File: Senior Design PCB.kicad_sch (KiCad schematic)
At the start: 49 parts, among them J1 Conn_01x02_Shielded, J2 Conn_01x02_Shielded, J3 Raspberry_Pi_Zero_2W, J4 Conn_01x02, J4(DISPLAY)1 Conn_01x09, J5 Conn_01x02, J6 Conn_01x02, U1 LM2596S-5, U2 MAX38890, U3 MCP3008

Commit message: More footprints added.
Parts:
- removed J1, J2: Conn_01x02_Shielded, symbol Connector_Generic_Shielded:Conn_01x02_Shielded
- removed J4(DISPLAY)1: Conn_01x09, symbol Connector_Generic:Conn_01x09
- removed U1: LM2596S-5, Package_TO_SOT_SMD:TO-263-5_TabPin3, symbol Regulator_Switching:LM2596S-5
- added H1, H2, H3, H4: MountingHole_Pad, MountingHole:MountingHole_3.2mm_M3_Pad, symbol Mechanical:MountingHole_Pad
- added J1, J2, TP2: Conn_01x02, Connector_PinHeader_2.54mm:PinHeader_1x02_P2.54mm_Vertical, symbol Connector_Generic:Conn_01x02
- added J7-A1: Conn_01x05, Connector_PinSocket_2.54mm:PinSocket_1x05_P2.54mm_Vertical, symbol Connector_Generic:Conn_01x05
- added J7-B1: Conn_01x04, Connector_PinSocket_2.54mm:PinSocket_1x04_P2.54mm_Vertical, symbol Connector_Generic:Conn_01x04
- added U1: LM2678SX-5.0/NOPB, TS7B, symbol AAA_Senior_Design:LM2678SX-5.0_NOPB
- BKB1, CAP1, ENB1, ENC1, FBCH1, FBCR1, FBS1, ISET1, LX1, RDY1, SYS1, VOUT1: footprint (none) -> Connector_Wire:SolderWire-1sqmm_1x02_P5.4mm_D1.4mm_OD2.7mm
- C1: renamed from C10; value 56uF -> 100uF; footprint (none) -> Capacitor_THT:CP_Radial_D8.0mm_P2.50mm
- C2: renamed from C12; footprint Capacitor_SMD:C_1206_3216Metric -> Capacitor_THT:CP_Radial_D5.0mm_P2.50mm
- C3: renamed from C7; footprint (none) -> Capacitor_THT:CP_Radial_D5.0mm_P2.00mm
- C5: renamed from C9; value 3.3nF -> 10nF; footprint (none) -> Capacitor_THT:CP_Radial_D10.0mm_P3.80mm
- C6: renamed from C13; footprint Capacitor_SMD:C_1206_3216Metric -> Capacitor_THT:CP_Radial_D5.0mm_P2.50mm
- C7: renamed from C11; value 330.0uF -> 220.0uF
- D1: value D_Schottky -> 40V; footprint (none) -> AAA_senior_design:D2PAK_STM
- L1: renamed from L2; value 47.0uH -> 15uH; footprint (none) -> AAA_senior_design:15uHInductor
- TP1: renamed from J4; footprint (none) -> Connector_Wire:SolderWire-1sqmm_1x02_P5.4mm_D1.4mm_OD2.7mm
- TP3: renamed from J5; footprint (none) -> Connector_Wire:SolderWire-1sqmm_1x02_P5.4mm_D1.4mm_OD2.7mm
- TP4: renamed from J6; footprint (none) -> Connector_Wire:SolderWire-1sqmm_1x02_P5.4mm_D1.4mm_OD2.7mm
- renumbered C4 to C10, C3 to C11, C5 to C12, C6 to C13, C8 to C4, C1 to C8, C2 to C9, L1 to L2, R5 to R1, R1 to R2, R2 to R3, R3 to R4, R4 to R5, R8 to R6, R9 to R7, R6 to R8, R7 to R9, U3 to U2, U2 to U3
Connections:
- net 12V: now also C2.2, U1.2 (VIN); no longer C1.1
- net 5V: now also U1.6 (FB); no longer C5.2
- net GND: now also H1.1, H2.1, H3.1, H4.1, J1.1 (Pin_1), J2.1 (Pin_1), J7-B1.4 (Pin_4), U1.4 (GND), U1.5 (NC), U1.8 (TAB); no longer C5.1
- net Vsig: now also J2.2 (Pin_2)
- net at D1.1 (K), L1.1: now also C5.2, U1.1 (VSW)
- net at TP1.1 (Pin_1): now also C1.1, J1.2 (Pin_2); no longer C2.2
- net at J3.2 (5V), U2.15 (Vref), U2.16 (Vdd): now also J7-A1.1 (Pin_1)
- net at J3.12 (SPI1_CE0): now also J7-A1.2 (Pin_2)
- net at J3.16 (RST): now also J7-A1.3 (Pin_3)
- net at J3.18 (GPIO24): now also J7-A1.4 (Pin_4)
- net at J3.29 (KEY1): now also J7-A1.5 (Pin_5)
- net at J3.31 (KEY0): now also J7-B1.1 (Pin_1)
- net at J3.38 (MOSI1): now also J7-B1.2 (Pin_2)
- net at J3.40 (SCLK1): now also J7-B1.3 (Pin_3)
- new net: C5.1, U1.3 (CB)
- new net: TP2.1 (Pin_1), TP2.2 (Pin_2), U1.7 (ON/~OFF)
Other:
- moved on the sheet: C1, C2, C5, C6, C7, CSCAP1, D1, L1, TP1

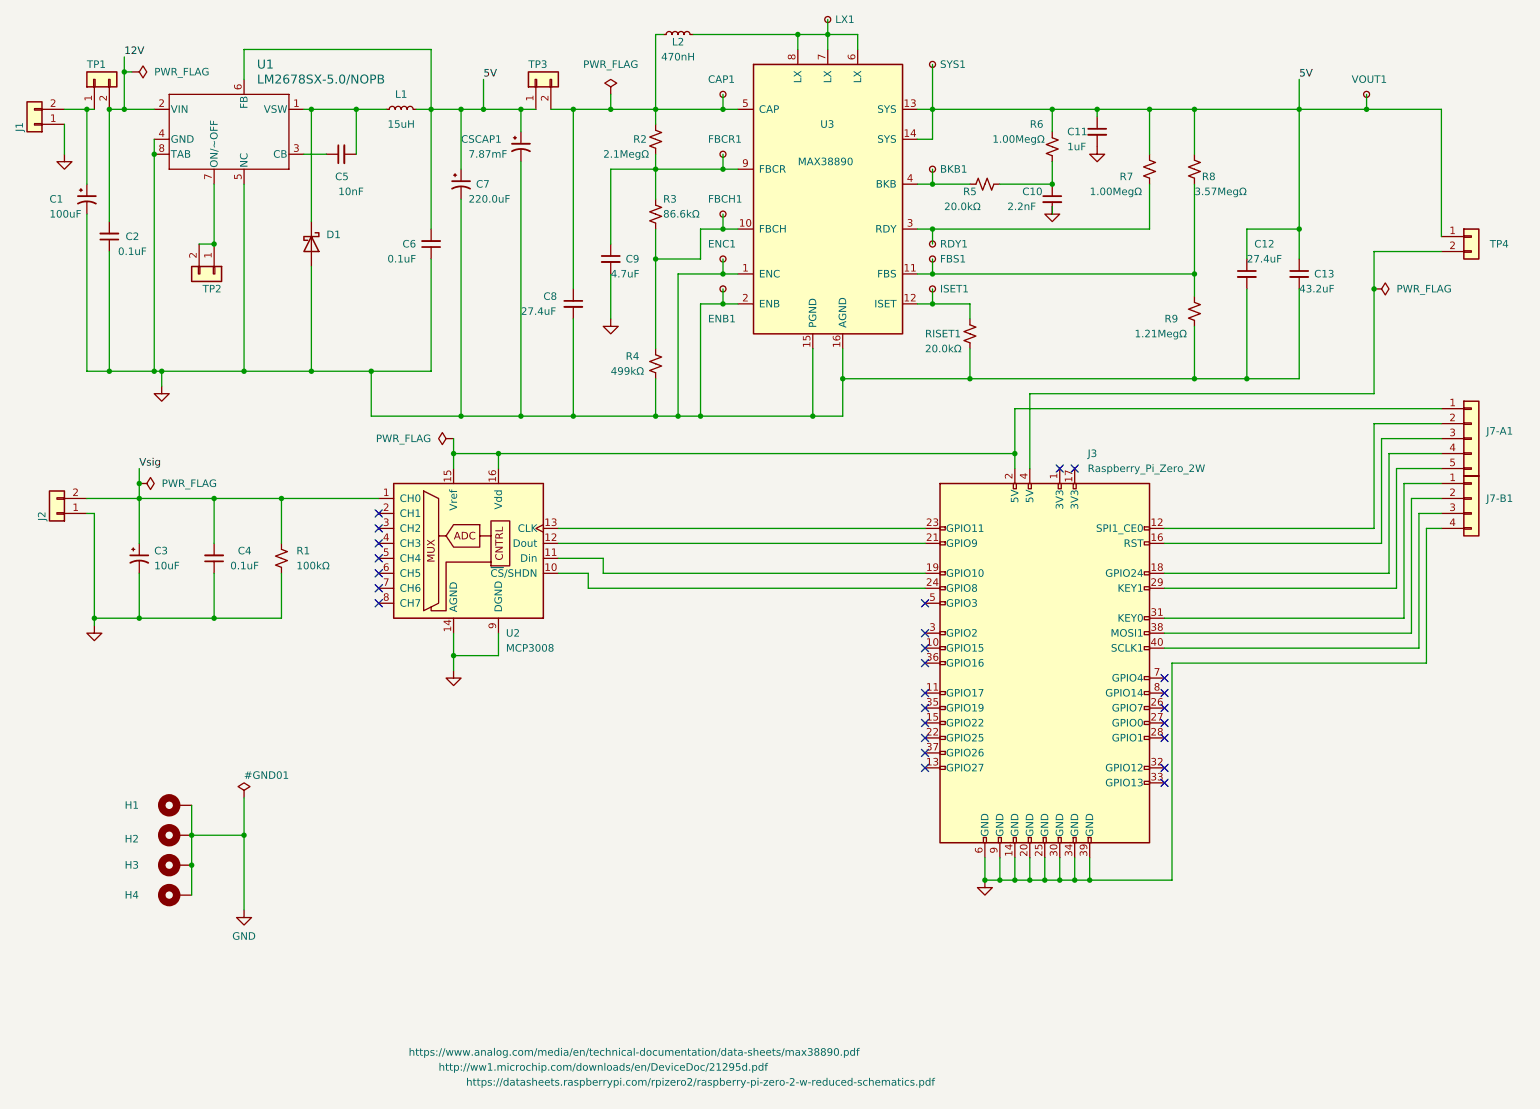
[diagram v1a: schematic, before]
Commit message: All footprints added.
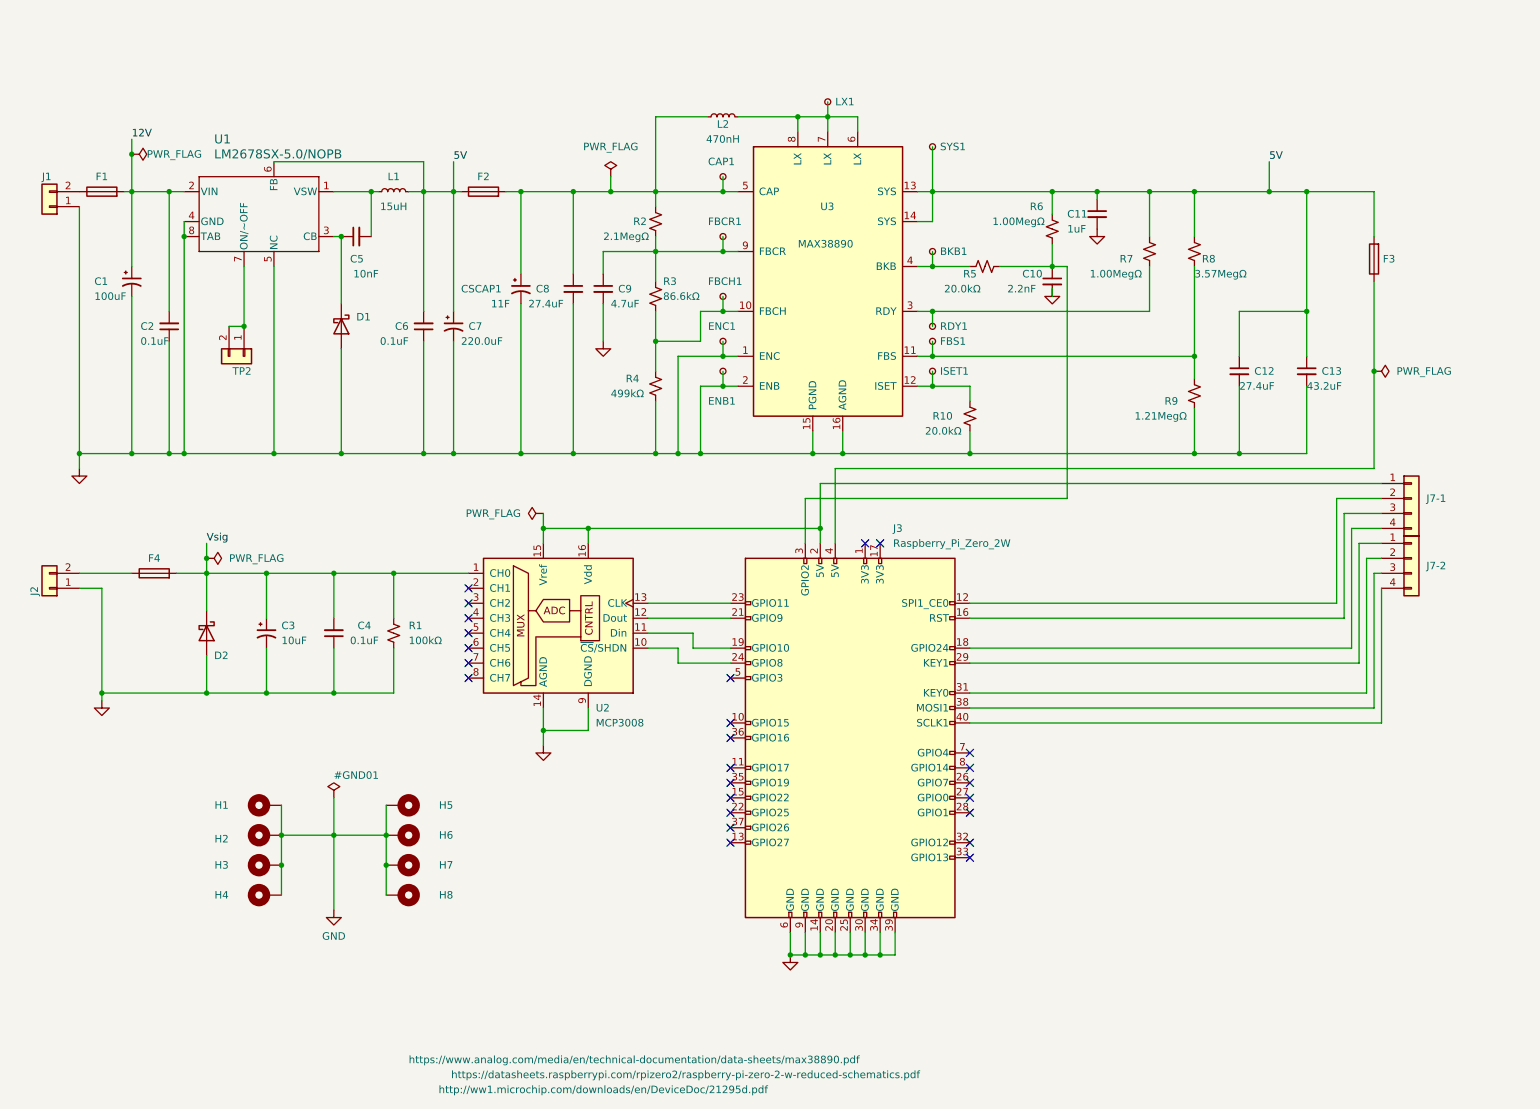
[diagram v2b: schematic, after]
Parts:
- removed J7-A1: Conn_01x05, Connector_PinSocket_2.54mm:PinSocket_1x05_P2.54mm_Vertical, symbol Connector_Generic:Conn_01x05
- removed J7-B1: Conn_01x04, Connector_PinSocket_2.54mm:PinSocket_1x04_P2.54mm_Vertical, symbol Connector_Generic:Conn_01x04
- removed TP1, TP3, TP4: Conn_01x02, Connector_Wire:SolderWire-1sqmm_1x02_P5.4mm_D1.4mm_OD2.7mm, symbol Connector_Generic:Conn_01x02
- removed VOUT1: TestPoint_Small, Connector_Wire:SolderWire-1sqmm_1x02_P5.4mm_D1.4mm_OD2.7mm, symbol Connector:TestPoint_Small
- added D2: 5.1V, Diode_THT:D_DO-34_SOD68_P10.16mm_Horizontal, symbol Device:D_Schottky
- added F1, F2, F3, F4: Fuse, AAA_senior_design:FUSE_4525, symbol Device:Fuse
- added H5, H6, H7, H8: MountingHole_Pad, MountingHole:MountingHole_3.5mm, symbol Mechanical:MountingHole_Pad
- added J7-1, J7-2: Conn_01x04, Connector_PinSocket_2.54mm:PinSocket_1x04_P2.54mm_Vertical, symbol Connector_Generic:Conn_01x04
- C10: footprint (none) -> AAA_senior_design:0603
- C11: footprint (none) -> AAA_senior_design:CAP_C0603_CND
- C12, C8: footprint (none) -> AAA_senior_design:CAPC3216X180N
- C13: footprint (none) -> AAA_senior_design:CAPC3225X270N
- C7: footprint (none) -> Capacitor_SMD:CP_Elec_8x6.9
- C9: footprint (none) -> AAA_senior_design:CAPC1608X87N
- CSCAP1: value 7.87mF -> 11F; footprint (none) -> Capacitor_THT:CP_Radial_D10.0mm_P5.00mm
- H1, H2, H3, H4: footprint MountingHole:MountingHole_3.2mm_M3_Pad -> MountingHole:MountingHole_5mm
- L2: footprint (none) -> AAA_senior_design:INDC2520X120N
- R1: footprint (none) -> Resistor_THT:R_Axial_DIN0207_L6.3mm_D2.5mm_P10.16mm_Horizontal
- R10: renamed from RISET1; footprint (none) -> AAA_senior_design:RESC1508X50N
- R2, R4, R5, R6, R7, R8, R9: footprint (none) -> AAA_senior_design:RESC1508X50N
- R3: footprint (none) -> AAA_senior_design:RES_ERJ3EKF4023V
- U1: footprint TS7B -> AAA_senior_design:TS7B
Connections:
- net 12V: now also C1.1, F1.2
- net 5V: now also F2.1, F3.2; no longer CSCAP1.1
- net GND: now also D2.2 (A), H5.1, H6.1, H7.1, H8.1
- net Vsig: now also D2.1 (K), F4.2; no longer J2.2 (Pin_2)
- net at C5.2, L1.1, U1.1 (VSW): no longer D1.1 (K)
- net at C5.1, U1.3 (CB): now also D1.1 (K)
- net at J1.2 (Pin_2): now also F1.1; no longer C1.1
- net at C10.1, R5.2, R6.2: now also J3.3 (GPIO2)
- net at J3.2 (5V), U2.15 (Vref), U2.16 (Vdd): now also J7-1.1 (Pin_1)
- net at J3.12 (SPI1_CE0): now also J7-1.2 (Pin_2)
- net at J3.16 (RST): now also J7-1.3 (Pin_3)
- net at J3.18 (GPIO24): now also J7-1.4 (Pin_4)
- net at J3.29 (KEY1): now also J7-2.1 (Pin_1)
- net at C8.1, CAP1.1, L2.1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: now also CSCAP1.1, F2.2
- net at J3.31 (KEY0): now also J7-2.2 (Pin_2)
- net at J3.38 (MOSI1): now also J7-2.3 (Pin_3)
- net at J3.4 (5V): now also F3.1
- net at J3.40 (SCLK1): now also J7-2.4 (Pin_4)
- new net: F4.1, J2.2 (Pin_2)
- no-connect marks 26 -> 25
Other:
- moved on the sheet: BKB1, C1, C10, C11, C12, C13, C2, C3, C4, C5, C6, C7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

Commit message: Fixed a few footprints. Started the design process. I'll start making branches after today.
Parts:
- BKB1, CAP1, ENB1, ENC1, FBCH1, FBCR1, FBS1, ISET1, LX1, RDY1, SYS1: footprint Connector_Wire:SolderWire-1sqmm_1x02_P5.4mm_D1.4mm_OD2.7mm -> TestPoint:TestPoint_Pad_D2.0mm
- H1, H2, H3, H4: footprint MountingHole:MountingHole_5mm -> MountingHole:MountingHole_5.3mm_M5_Pad
- H5, H6, H7, H8: footprint MountingHole:MountingHole_3.5mm -> MountingHole:MountingHole_3.5mm_Pad
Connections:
- net at C5.2, L1.1, U1.1 (VSW): now also D1.1 (K)
- net at C5.1, U1.3 (CB): no longer D1.1 (K)
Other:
- moved on the sheet: C5, C6, C7, C8, CSCAP1, F2, L1

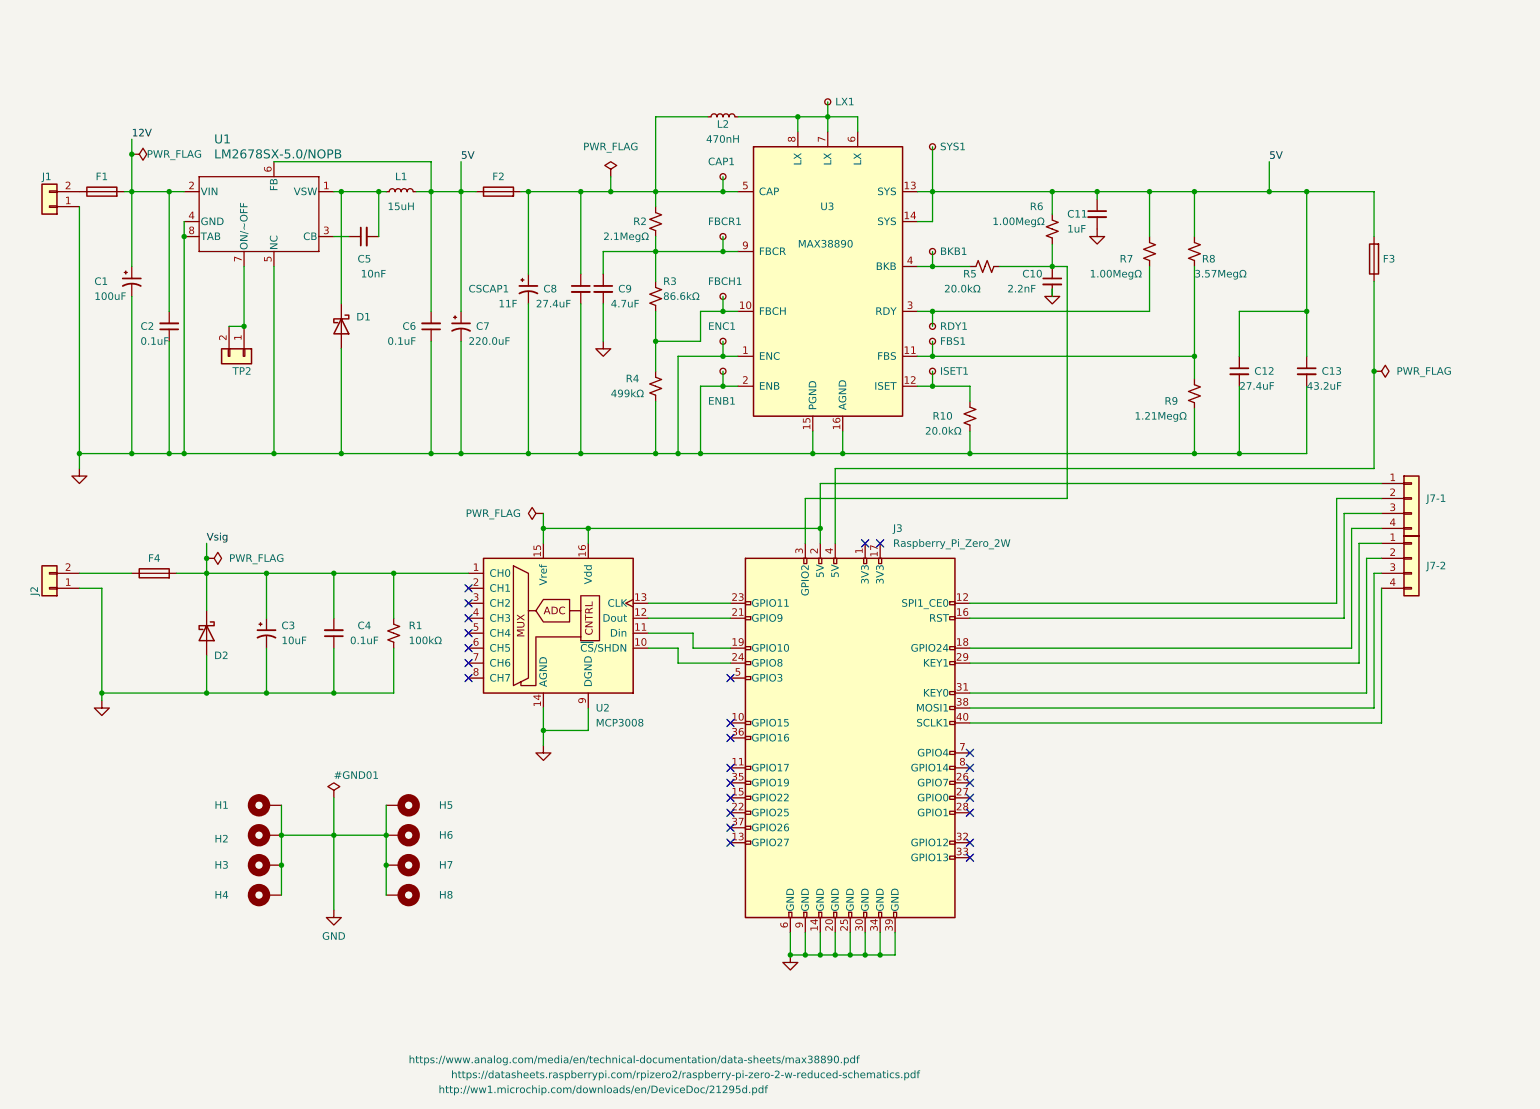
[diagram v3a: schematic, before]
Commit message: Laid fourth draft of traces and passed all drc checks. gnd planes added and the mounting holes are added, as well. Remaining steps are to add leds or 50k ohm resistor.
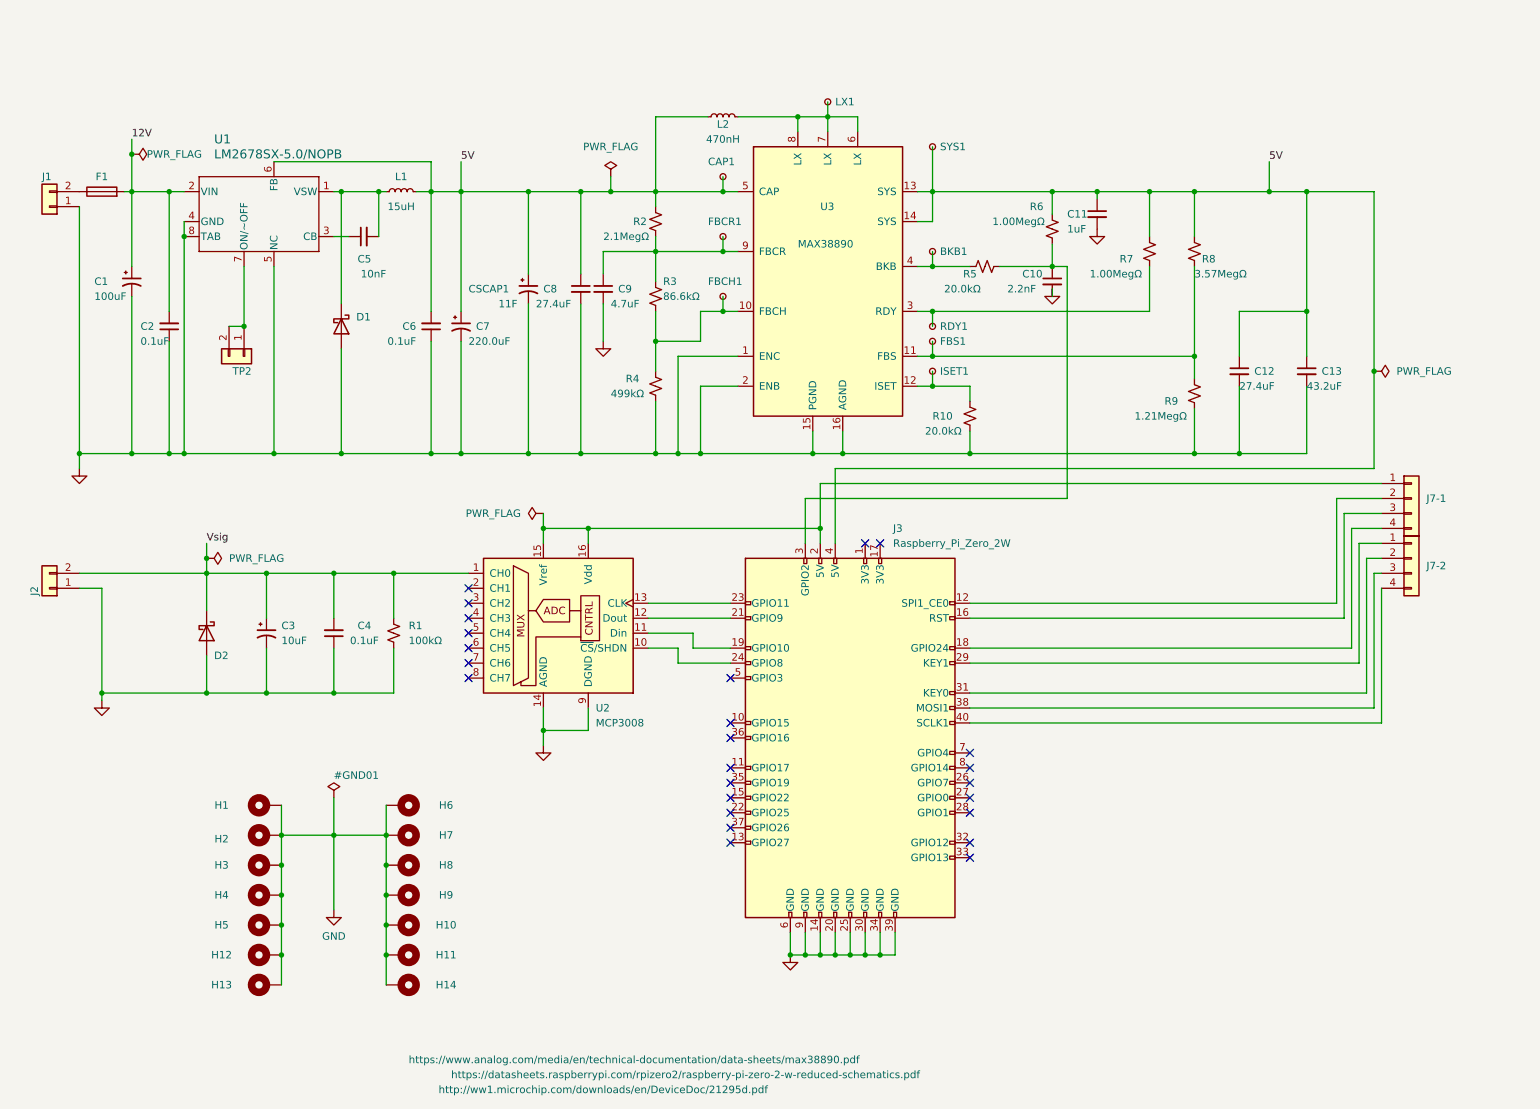
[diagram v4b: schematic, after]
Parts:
- removed ENB1, ENC1: TestPoint_Small, TestPoint:TestPoint_Pad_D2.0mm, symbol Connector:TestPoint_Small
- removed F2, F3, F4: Fuse, AAA_senior_design:FUSE_4525, symbol Device:Fuse
- added H10, H11, H12, H13, H14, H9: MountingHole_Pad, MountingHole:MountingHole_3.2mm_M3_Pad, symbol Mechanical:MountingHole_Pad
- H1, H2, H3, H4: footprint MountingHole:MountingHole_5.3mm_M5_Pad -> MountingHole:MountingHole_3.2mm_M3_Pad
- H5, H6, H7, H8: footprint MountingHole:MountingHole_3.5mm_Pad -> MountingHole:MountingHole_3.2mm_M3_Pad
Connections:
- net 5V: now also C8.1, CAP1.1, CSCAP1.1, J3.4 (5V), L2.1, R2.1, U3.5 (CAP)
- net GND: now also H10.1, H11.1, H12.1, H13.1, H14.1, H9.1
- net Vsig: now also J2.2 (Pin_2)
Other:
- moved on the sheet: H5, H6, H7, H8
